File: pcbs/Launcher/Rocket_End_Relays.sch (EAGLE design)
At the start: 39 parts, among them IC2 LM2576T-ADJ, K4 LD105, K5 LD105, K6 LD105, K7 LD105, T1 BC547, T2 BC547, T3 BC547, T4 BC547, T5 BC547, U1 ARDUINO-MEGAPRO-5V, X1 22-23-2041, X2 22-23-2041, X3 22-23-2021, X7 22-23-2021

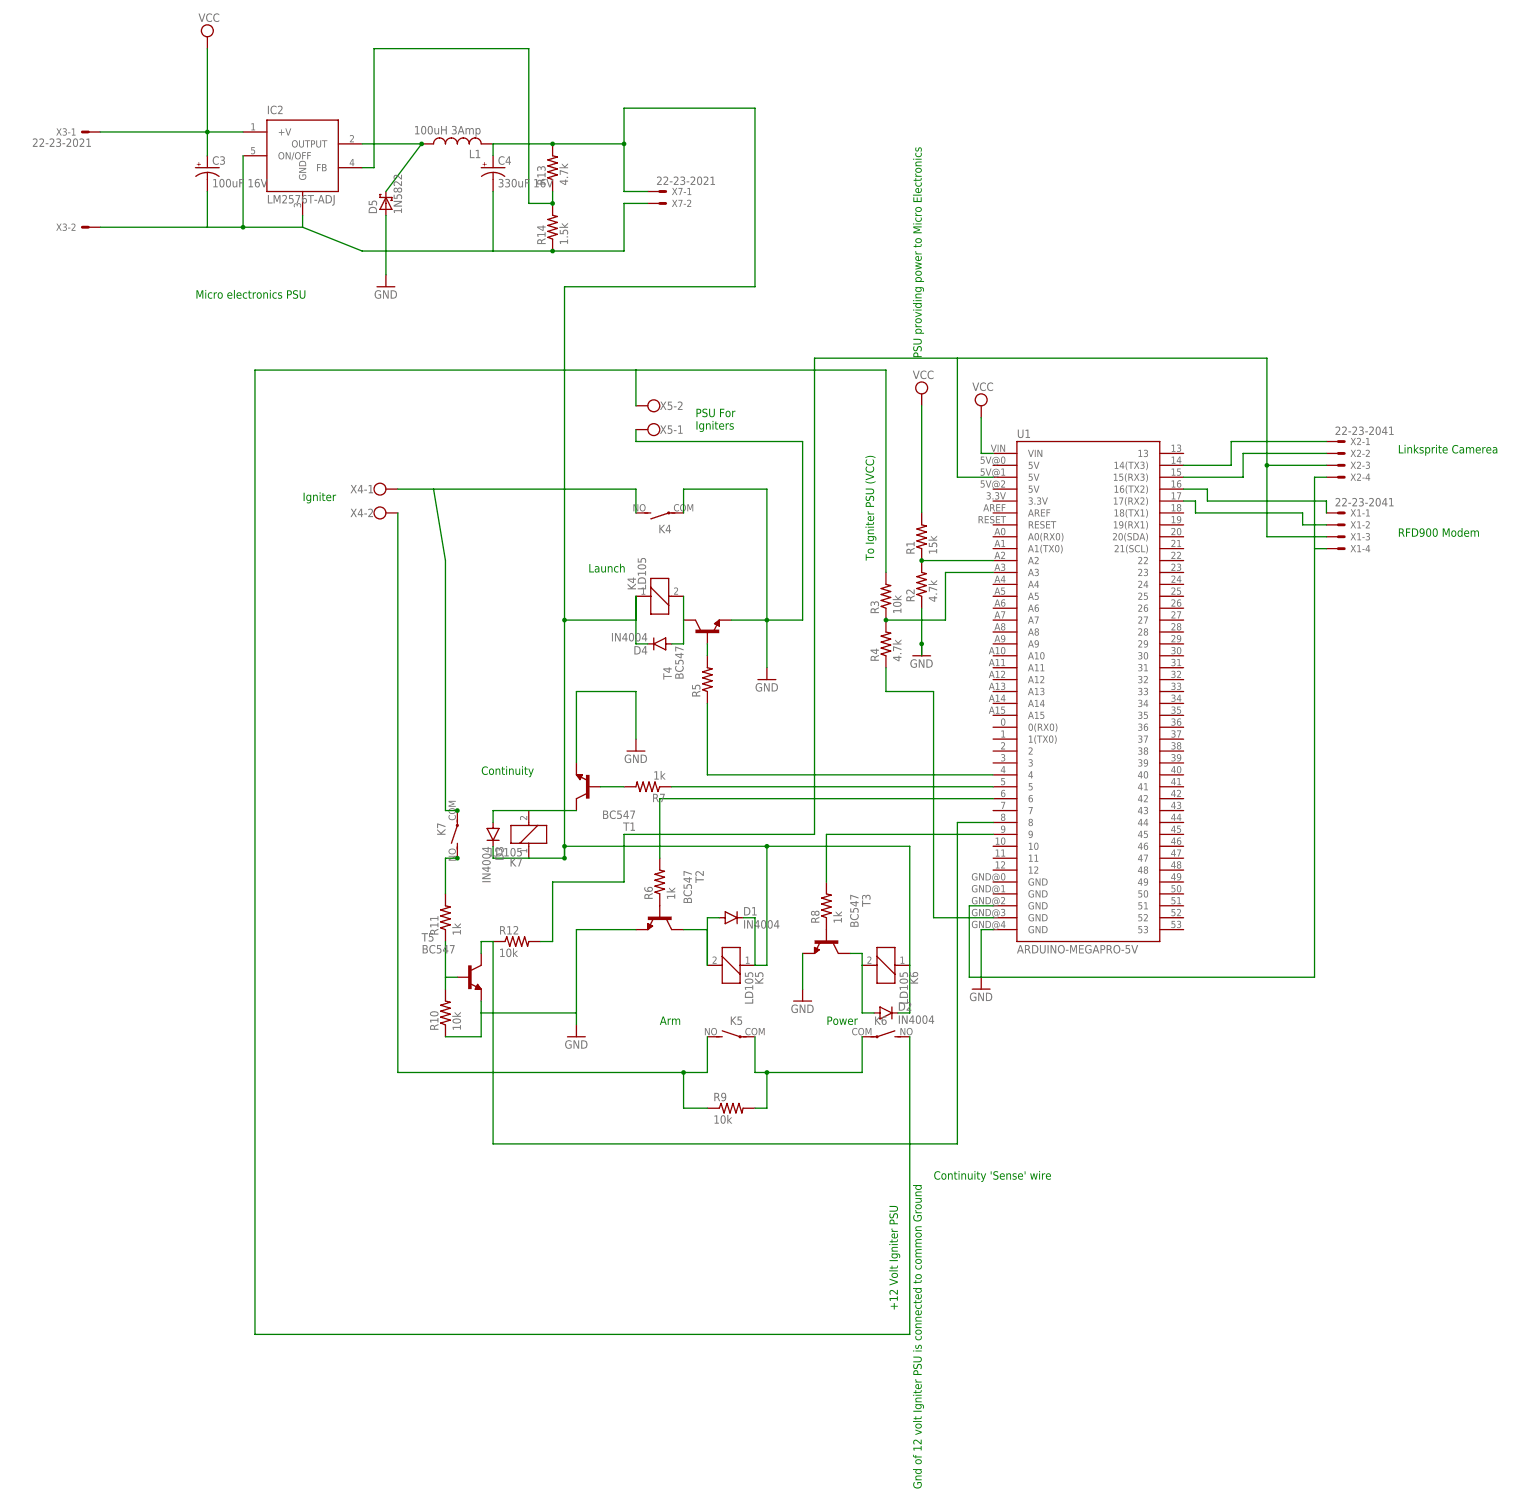
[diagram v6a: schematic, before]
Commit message: * Added library deps * Modified to use an edited version of library, removing most of digital pins * adding in connector pins to put right angle 2 lots of 2x4 pins
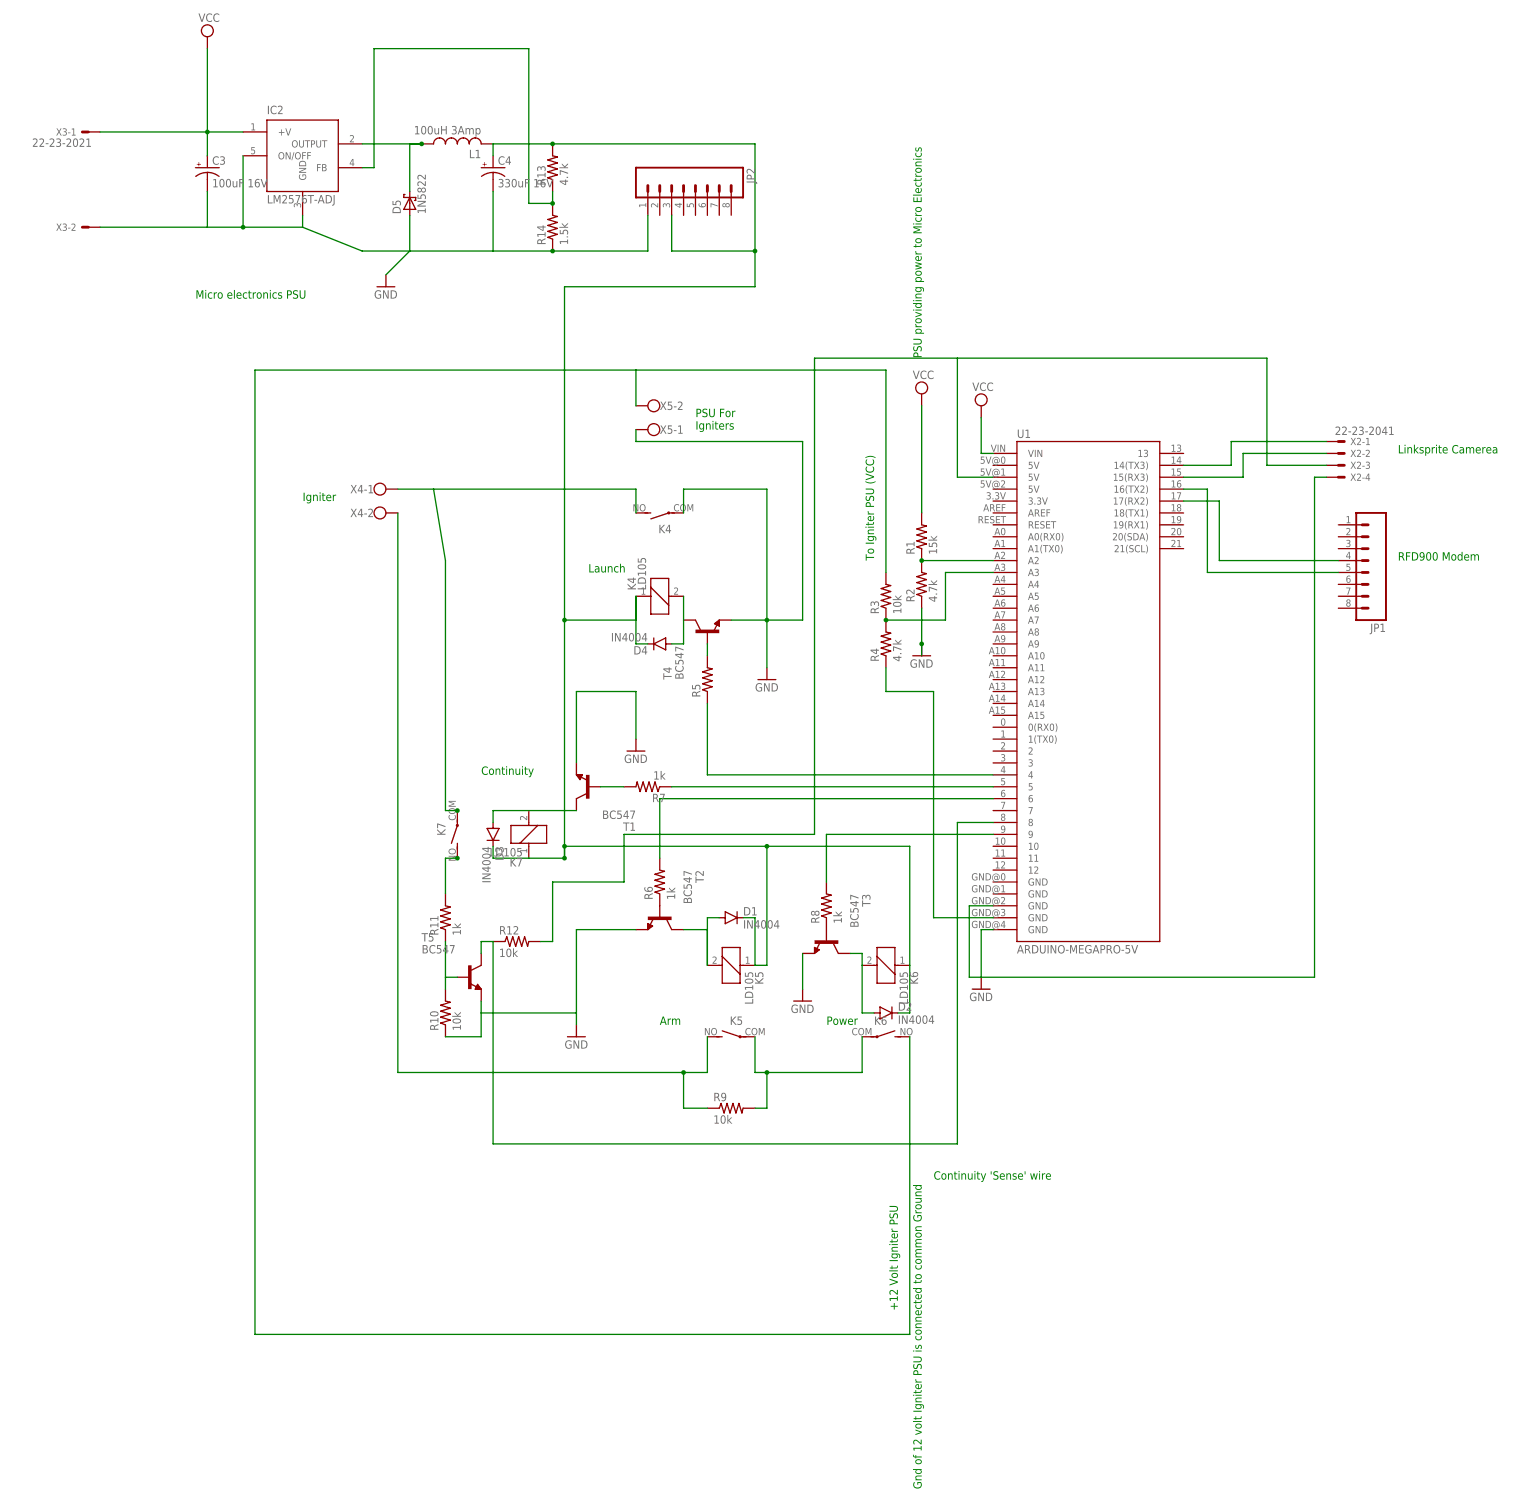
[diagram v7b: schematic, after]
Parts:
- removed X1: 22-23-2041, con-molex:22-23-2041
- removed X7: 22-23-2021, con-molex:22-23-2021
- added JP1, JP2: (no value), SparkFun-Connectors:M08
- U1: device SparkFun-Boards:ARDUINO-MEGAPRO-5V -> JoeMega_Ether_Edited:ARDUINO-MEGAPRO-5V
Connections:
- net N$1: now also JP1.5; no longer X1-1.S
- net N$16: no longer X1-4.S
- net N$2: now also JP1.4; no longer X1-2.S
- net N$23: no longer X1-3.S
- net N$33: now also JP2.1; no longer X7-2.S
- net N$5: now also JP2.3; no longer X7-1.S
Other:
- moved on the sheet: D5
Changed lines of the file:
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@@
 </classes>
 <parts>
-<part name="U1" library="SparkFun-Boards" deviceset="ARDUINO-MEGA" device="PRO-5V"/>
-<part name="X1" library="con-molex" deviceset="22-23-2041" device=""/>
+<part name="U1" library="JoeMega_Ether_Edited" deviceset="ARDUINO-MEGA" device="PRO-5V"/>
 <part name="X2" library="con-molex" deviceset="22-23-2041" device=""/>
 <part name="R1" library="rcl" deviceset="R-US_" device="0204/7" value="15k"/>
@@
 <part name="R14" library="resistor" deviceset="R-US_" device="0207/7" value="1.5k"/>
 <part name="D5" library="diode" deviceset="1N5908" device="" value="1N5822"/>
-<part name="X7" library="con-molex" deviceset="22-23-2021" device=""/>
 <part name="SUPPLY2" library="supply2" deviceset="VCC" device=""/>
 <part name="R10" library="rcl" deviceset="R-US_" device="0207/7" value="10k"/>
 <part name="X5" library="con-wago-500" deviceset="W237-102" device=""/>
 <part name="X4" library="con-wago-500" deviceset="W237-102" device=""/>
+<part name="JP1" library="SparkFun-Connectors" deviceset="M08" device=""/>
+<part name="JP2" library="SparkFun-Connectors" deviceset="M08" device=""/>
 </parts>
 <sheets>
@@
 <plain>
 <text x="104.14" y="104.14" size="1.778" layer="91">Linksprite Camerea</text>
-<text x="104.14" y="86.36" size="1.778" layer="91">RFD900 Modem</text>
+<text x="104.14" y="81.28" size="1.778" layer="91">RFD900 Modem</text>
 <text x="-7.62" y="81.28" size="1.778" layer="91" rot="R90">To Igniter PSU (VCC)</text>
 <text x="-68.58" y="78.74" size="1.778" layer="91">Launch</text>
@@
 <instances>
 <instance part="U1" gate="G$1" x="38.1" y="53.34"/>
-<instance part="X1" gate="-1" x="91.44" y="91.44"/>
-<instance part="X1" gate="-2" x="91.44" y="88.9"/>
-<instance part="X1" gate="-3" x="91.44" y="86.36"/>
-<instance part="X1" gate="-4" x="91.44" y="83.82"/>
 <instance part="X2" gate="-1" x="91.44" y="106.68"/>
 <instance part="X2" gate="-2" x="91.44" y="104.14"/>
@@
 <instance part="R13" gate="G$1" x="-76.2" y="165.1" rot="R90"/>
 <instance part="R14" gate="G$1" x="-76.2" y="152.4" rot="R90"/>
-<instance part="D5" gate="1" x="-111.76" y="157.48" rot="R90"/>
-<instance part="X7" gate="-1" x="-53.34" y="160.02"/>
-<instance part="X7" gate="-2" x="-53.34" y="157.48"/>
+<instance part="D5" gate="1" x="-106.68" y="157.48" rot="R90"/>
 <instance part="SUPPLY2" gate="G$1" x="-149.86" y="193.04"/>
 <instance part="R10" gate="G$1" x="-99.06" y="-15.24" rot="R90"/>
@@
 <instance part="X4" gate="-1" x="-114.3" y="96.52"/>
 <instance part="X4" gate="-2" x="-114.3" y="91.44"/>
+<instance part="JP1" gate="G$1" x="96.52" y="81.28" rot="R180"/>
+<instance part="JP2" gate="G$1" x="-48.26" y="160.02" rot="R270"/>
 </instances>
 <busses>
@@
 <wire x1="-149.86" y1="152.4" x2="-142.24" y2="152.4" width="0.1524" layer="91"/>
 <wire x1="-129.54" y1="152.4" x2="-116.84" y2="147.32" width="0.1524" layer="91"/>
-<wire x1="-116.84" y1="147.32" x2="-111.76" y2="147.32" width="0.1524" layer="91"/>
-<wire x1="-111.76" y1="147.32" x2="-88.9" y2="147.32" width="0.1524" layer="91"/>
+<wire x1="-116.84" y1="147.32" x2="-106.68" y2="147.32" width="0.1524" layer="91"/>
+<wire x1="-106.68" y1="147.32" x2="-88.9" y2="147.32" width="0.1524" layer="91"/>
 <wire x1="-142.24" y1="152.4" x2="-129.54" y2="152.4" width="0.1524" layer="91"/>
 <pinref part="C4" gate="G$1" pin="-"/>
 <wire x1="-88.9" y1="160.02" x2="-88.9" y2="147.32" width="0.1524" layer="91"/>
 <pinref part="D5" gate="1" pin="A"/>
-<wire x1="-111.76" y1="154.94" x2="-111.76" y2="147.32" width="0.1524" layer="91"/>
+<wire x1="-106.68" y1="154.94" x2="-106.68" y2="147.32" width="0.1524" layer="91"/>
 <wire x1="-88.9" y1="147.32" x2="-76.2" y2="147.32" width="0.1524" layer="91"/>
-<wire x1="-76.2" y1="147.32" x2="-60.96" y2="147.32" width="0.1524" layer="91"/>
-<wire x1="-60.96" y1="147.32" x2="-60.96" y2="157.48" width="0.1524" layer="91"/>
-<pinref part="X7" gate="-2" pin="S"/>
-<wire x1="-60.96" y1="157.48" x2="-55.88" y2="157.48" width="0.1524" layer="91"/>
+<wire x1="-76.2" y1="147.32" x2="-55.88" y2="147.32" width="0.1524" layer="91"/>
 <pinref part="C3" gate="G$1" pin="-"/>
 <wire x1="-149.86" y1="160.02" x2="-149.86" y2="152.4" width="0.1524" layer="91"/>
@@
 <wire x1="-149.86" y1="152.4" x2="-172.72" y2="152.4" width="0.1524" layer="91"/>
 <pinref part="GND11" gate="1" pin="GND"/>
-<wire x1="-111.76" y1="147.32" x2="-111.76" y2="142.24" width="0.1524" layer="91"/>
+<wire x1="-106.68" y1="147.32" x2="-111.76" y2="142.24" width="0.1524" layer="91"/>
 <pinref part="IC2" gate="G$1" pin="GND"/>
 <wire x1="-129.54" y1="152.4" x2="-129.54" y2="154.94" width="0.1524" layer="91"/>
+<pinref part="JP2" gate="G$1" pin="1"/>
+<wire x1="-55.88" y1="154.94" x2="-55.88" y2="147.32" width="0.1524" layer="91"/>
 </segment>
 </net>
@@
 <net name="N$1" class="0">
 <segment>
-<pinref part="X1" gate="-1" pin="S"/>
-<wire x1="88.9" y1="91.44" x2="88.9" y2="93.98" width="0.1524" layer="91"/>
-<wire x1="88.9" y1="93.98" x2="63.5" y2="93.98" width="0.1524" layer="91"/>
 <pinref part="U1" gate="G$1" pin="16(TX2)"/>
-<wire x1="63.5" y1="93.98" x2="63.5" y2="96.52" width="0.1524" layer="91"/>
+<wire x1="63.5" y1="78.74" x2="63.5" y2="96.52" width="0.1524" layer="91"/>
 <wire x1="63.5" y1="96.52" x2="58.42" y2="96.52" width="0.1524" layer="91"/>
+<pinref part="JP1" gate="G$1" pin="5"/>
+<wire x1="63.5" y1="78.74" x2="91.44" y2="78.74" width="0.1524" layer="91"/>
 </segment>
 </net>
@@
 <segment>
 <pinref part="U1" gate="G$1" pin="17(RX2)"/>
-<wire x1="58.42" y1="93.98" x2="60.96" y2="93.98" width="0.1524" layer="91"/>
-<wire x1="60.96" y1="93.98" x2="60.96" y2="91.44" width="0.1524" layer="91"/>
-<wire x1="60.96" y1="91.44" x2="83.82" y2="91.44" width="0.1524" layer="91"/>
-<pinref part="X1" gate="-2" pin="S"/>
-<wire x1="83.82" y1="91.44" x2="83.82" y2="88.9" width="0.1524" layer="91"/>
-<wire x1="83.82" y1="88.9" x2="88.9" y2="88.9" width="0.1524" layer="91"/>
+<wire x1="58.42" y1="93.98" x2="66.04" y2="93.98" width="0.1524" layer="91"/>
+<wire x1="66.04" y1="93.98" x2="66.04" y2="81.28" width="0.1524" layer="91"/>
+<pinref part="JP1" gate="G$1" pin="4"/>
+<wire x1="66.04" y1="81.28" x2="91.44" y2="81.28" width="0.1524" layer="91"/>
 </segment>
 </net>
@@
 <wire x1="0" y1="-15.24" x2="-2.54" y2="-15.24" width="0.1524" layer="91"/>
 <wire x1="-73.66" y1="139.7" x2="-33.02" y2="139.7" width="0.1524" layer="91"/>
-<wire x1="-33.02" y1="139.7" x2="-33.02" y2="177.8" width="0.1524" layer="91"/>
-<wire x1="-33.02" y1="177.8" x2="-60.96" y2="177.8" width="0.1524" layer="91"/>
+<wire x1="-33.02" y1="139.7" x2="-33.02" y2="147.32" width="0.1524" layer="91"/>
+<wire x1="-33.02" y1="147.32" x2="-33.02" y2="170.18" width="0.1524" layer="91"/>
+<wire x1="-33.02" y1="170.18" x2="-76.2" y2="170.18" width="0.1524" layer="91"/>
 <pinref part="L1" gate="G$1" pin="2"/>
 <pinref part="C4" gate="G$1" pin="+"/>
@@
 <wire x1="-88.9" y1="167.64" x2="-88.9" y2="170.18" width="0.1524" layer="91"/>
 <pinref part="R13" gate="G$1" pin="2"/>
-<wire x1="-76.2" y1="170.18" x2="-60.96" y2="170.18" width="0.1524" layer="91"/>
-<wire x1="-60.96" y1="170.18" x2="-60.96" y2="160.02" width="0.1524" layer="91"/>
-<pinref part="X7" gate="-1" pin="S"/>
-<wire x1="-60.96" y1="160.02" x2="-55.88" y2="160.02" width="0.1524" layer="91"/>
-<wire x1="-60.96" y1="177.8" x2="-60.96" y2="170.18" width="0.1524" layer="91"/>
 <junction x="-76.2" y="170.18"/>
-<junction x="-60.96" y="170.18"/>
+<pinref part="JP2" gate="G$1" pin="3"/>
+<wire x1="-50.8" y1="154.94" x2="-50.8" y2="147.32" width="0.1524" layer="91"/>
+<wire x1="-50.8" y1="147.32" x2="-33.02" y2="147.32" width="0.1524" layer="91"/>
+<junction x="-33.02" y="147.32"/>
 </segment>
 </net>
 <net name="N$16" class="0">
 <segment>
-<pinref part="X1" gate="-4" pin="S"/>
-<wire x1="88.9" y1="83.82" x2="86.36" y2="83.82" width="0.1524" layer="91"/>
 <pinref part="X2" gate="-4" pin="S"/>
 <wire x1="88.9" y1="99.06" x2="86.36" y2="99.06" width="0.1524" layer="91"/>
-<wire x1="86.36" y1="99.06" x2="86.36" y2="83.82" width="0.1524" layer="91"/>
-<wire x1="86.36" y1="83.82" x2="86.36" y2="-7.62" width="0.1524" layer="91"/>
+<wire x1="86.36" y1="99.06" x2="86.36" y2="-7.62" width="0.1524" layer="91"/>
 <wire x1="86.36" y1="-7.62" x2="12.7" y2="-7.62" width="0.1524" layer="91"/>
 <wire x1="12.7" y1="-7.62" x2="12.7" y2="7.62" width="0.1524" layer="91"/>
@@
 <pinref part="L1" gate="G$1" pin="1"/>
 <pinref part="D5" gate="1" pin="C"/>
-<wire x1="-111.76" y1="160.02" x2="-104.14" y2="170.18" width="0.1524" layer="91"/>
+<wire x1="-106.68" y1="160.02" x2="-106.68" y2="170.18" width="0.1524" layer="91"/>
+<wire x1="-106.68" y1="170.18" x2="-104.14" y2="170.18" width="0.1524" layer="91"/>
 <junction x="-104.14" y="170.18"/>
 </segment>
@@
 <wire x1="-60.96" y1="22.86" x2="-20.32" y2="22.86" width="0.1524" layer="91"/>
 <wire x1="-20.32" y1="22.86" x2="-20.32" y2="124.46" width="0.1524" layer="91"/>
-<pinref part="X1" gate="-3" pin="S"/>
-<wire x1="88.9" y1="86.36" x2="76.2" y2="86.36" width="0.1524" layer="91"/>
-<wire x1="76.2" y1="86.36" x2="76.2" y2="101.6" width="0.1524" layer="91"/>
 <wire x1="76.2" y1="101.6" x2="76.2" y2="124.46" width="0.1524" layer="91"/>
 <pinref part="X2" gate="-3" pin="S"/>
 <wire x1="88.9" y1="101.6" x2="76.2" y2="101.6" width="0.1524" layer="91"/>
-<junction x="76.2" y="101.6"/>
 <wire x1="10.16" y1="99.06" x2="10.16" y2="124.46" width="0.1524" layer="91"/>
 <wire x1="10.16" y1="124.46" x2="76.2" y2="124.46" width="0.1524" layer="91"/>

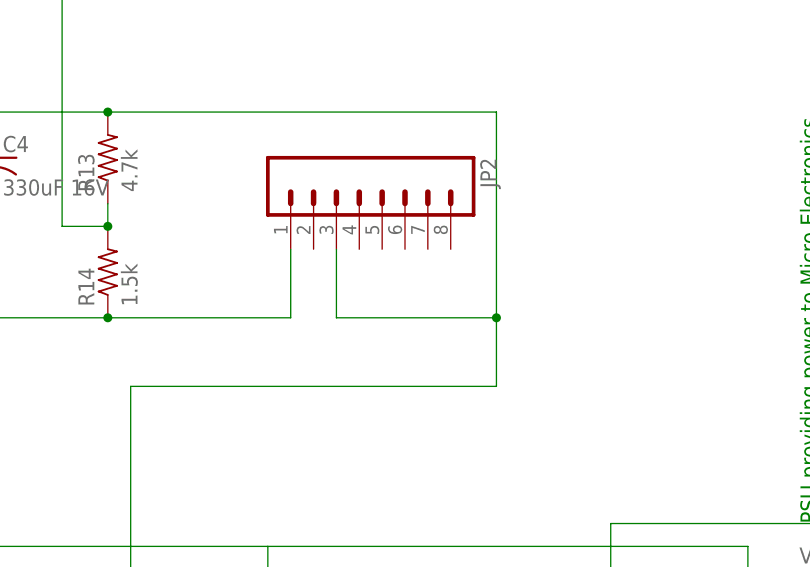
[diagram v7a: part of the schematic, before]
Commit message: * Put 5volt on pin NEXT to ground.
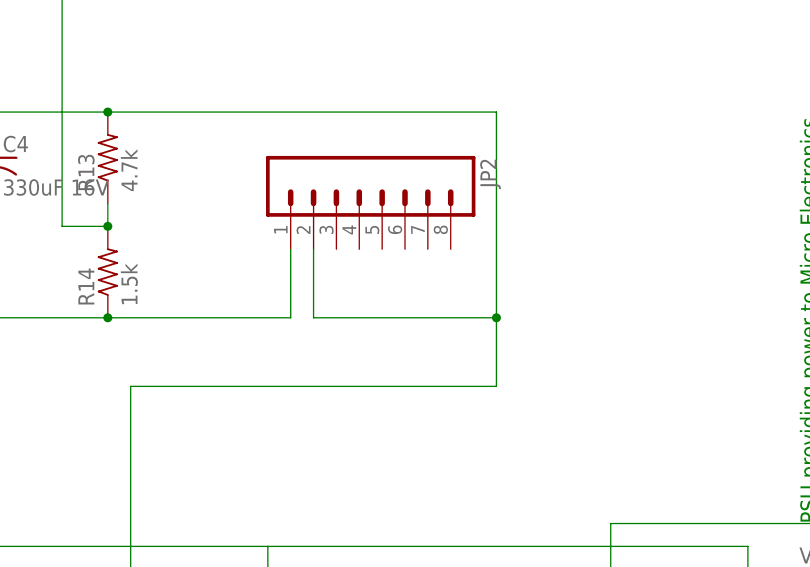
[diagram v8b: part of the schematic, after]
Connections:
- net N$5: now also JP2.2; no longer JP2.3
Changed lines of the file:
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@@
 <?xml version="1.0" encoding="utf-8"?>
 <!DOCTYPE eagle SYSTEM "eagle.dtd">
-<eagle version="7.1.0">
+<eagle version="7.3.0">
 <drawing>
 <settings>
@@
 <pinref part="R13" gate="G$1" pin="2"/>
 <junction x="-76.2" y="170.18"/>
-<pinref part="JP2" gate="G$1" pin="3"/>
-<wire x1="-50.8" y1="154.94" x2="-50.8" y2="147.32" width="0.1524" layer="91"/>
-<wire x1="-50.8" y1="147.32" x2="-33.02" y2="147.32" width="0.1524" layer="91"/>
+<wire x1="-53.34" y1="147.32" x2="-33.02" y2="147.32" width="0.1524" layer="91"/>
 <junction x="-33.02" y="147.32"/>
-</segment>
-</net>
+<pinref part="JP2" gate="G$1" pin="2"/>
+<wire x1="-53.34" y1="147.32" x2="-53.34" y2="154.94" width="0.1524" layer="91"/>
+</segment>
+</net>
